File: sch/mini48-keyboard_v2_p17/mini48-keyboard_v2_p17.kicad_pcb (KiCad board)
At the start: 2 copper layers, 232 x 76 mm, 120 parts, among them SW1 SW_Push, SW10 SW_Push, SW11 SW_Push, SW12 SW_Push, SW13 SW_Push, SW14 SW_Push, SW15 SW_Push, SW16 SW_Push, SW17 SW_Push, SW18 SW_Push, SW19 SW_Push, SW2 SW_Push, SW20 SW_Push, SW21 SW_Push, SW22 SW_Push, SW23 SW_Push, SW24 SW_Push, SW25 SW_Push, SW26 SW_Push, SW27 SW_Push, SW28 SW_Push, SW29 SW_Push, SW3 SW_Push, SW30 SW_Push, SW31 SW_Push, SW32 SW_Push, SW33 SW_Push, SW34 SW_Push, SW35 SW_Push, SW36 SW_Push, SW37 SW_Push, SW38 SW_Push, SW39 SW_Push, SW4 SW_Push, SW40 SW_Push, SW41 SW_Push, SW42 SW_Push, SW43 SW_Push, SW44 SW_Push, SW45 SW_Push, SW46 SW_Push, SW47 SW_Push, SW48 SW_Push, SW5 SW_Push, SW6 SW_Push, SW7 SW_Push, SW8 SW_Push, SW9 SW_Push

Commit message: ざっくり配線しました。 pico と  ae-rp2040 を選択できるようにしました。
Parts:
- removed the REF** at (59.0, 57.0)
- removed the REF** at (210.0, 128.0)
- added D49: PMEG40T20ER, Diode_SMD:Nexperia_CFP3_SOD-123W, F.Cu at (250.6, 32.0)
- added J1: Conn_01x20, Connector_PinHeader_2.54mm:PinHeader_1x20_P2.54mm_Vertical, F.Cu at (139.1, 84.0)
- added J2: Conn_01x02, Connector_JST:JST_PH_B2B-PH-K_1x02_P2.00mm_Vertical, F.Cu at (250.8, 26.6)
- added U2: Pico, my_pico:pico_no_dbg_smd_th_p0.85, F.Cu at (221.9, 62.9)
- U1: footprint ae-rp2040:AE-RP2040 -> ae-rp2040:AE-RP2040_p0.85; moved to F.Cu
- moved REF** 195.3 mm to (111.0, 175.0)
- moved REF** 172.0 mm to (103.0, 174.0)
- moved REF** 168.3 mm to (132.0, 174.0)
- moved REF** 153.9 mm to (91.0, 174.0)
- moved REF** 138.3 mm to (79.0, 174.0)
- moved REF** 135.3 mm to (145.0, 187.0)
- moved REF** 131.6 mm to (119.0, 188.0)
- moved REF** 126.2 mm to (67.0, 174.0)
- moved REF** 120.5 mm to (98.0, 188.0)
- moved REF** 119.0 mm to (53.0, 174.0)
- moved REF** 116.5 mm to (41.0, 174.0)
- moved REF** 113.7 mm to (132.0, 187.0)
- moved REF** 110.5 mm to (78.0, 188.0)
- moved REF** 105.9 mm to (22.0, 178.0)
- moved REF** 103.0 mm to (57.0, 188.0)
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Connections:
- net /COL0 renamed /GPIO15
- net /COL1 renamed /GPIO14
- net /COL10 renamed /GPIO20
- net /COL11 renamed /GPIO21
- net /COL2 renamed /GPIO13
- net /COL3 renamed /GPIO12
- net /COL4 renamed /GPIO11
- net /COL5 renamed /GPIO10
- net /COL6 renamed /GPIO16
- net /COL7 renamed /GPIO17
- net /COL8 renamed /GPIO18
- net /COL9 renamed /GPIO19
- net /ROW0 renamed /GPIO2
- net /ROW1 renamed /GPIO3
- net /ROW2 renamed /GPIO4
- net /ROW3 renamed /GPIO5
- U1 pad 10: unconnected-(U1-GPIO8-Pad10) -> /GPIO8
- U1 pad 11: unconnected-(U1-GPIO9-Pad11) -> /GPIO9
- U1 pad 2: unconnected-(U1-GPIO0-Pad2) -> /GPIO0
- U1 pad 25: unconnected-(U1-GPIO22-Pad25) -> /GPIO22
- U1 pad 29: unconnected-(U1-GPIO26-Pad29) -> /GPIO26
- U1 pad 3: unconnected-(U1-GPIO1-Pad3) -> /GPIO1
- U1 pad 30: unconnected-(U1-GPIO27-Pad30) -> /GPIO27
- U1 pad 31: unconnected-(U1-GPIO28-Pad31) -> /GPIO28
- U1 pad 34: +3.3V -> unconnected-(U1-+3.3V-Pad34)
- U1 pad 8: unconnected-(U1-GPIO6-Pad8) -> /GPIO6
- U1 pad 9: unconnected-(U1-GPIO7-Pad9) -> /GPIO7
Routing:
- net /GPIO5: track 244.5 -> 355.3 mm
- net /GPIO2: track 322.2 -> 226.0 mm
- net /GPIO12: track 210.3 -> 129.5 mm, vias 1 -> 0
- net /GPIO11: track 187.8 -> 115.7 mm, vias 1 -> 0
- net /GPIO21: track 68.0 -> 138.6 mm
- net /GPIO15: track 244.6 -> 175.3 mm, vias 1 -> 0
- net /GPIO10: track 169.8 -> 101.0 mm, vias 1 -> 0
- net /GPIO13: track 211.7 -> 144.6 mm, vias 1 -> 0
- net /GPIO14: track 226.9 -> 161.3 mm, vias 1 -> 0
- net /GPIO4: track 275.5 -> 340.3 mm
- net /GPIO16: track 149.7 -> 93.0 mm, vias 1 -> 0
- net /GPIO20: track 69.3 -> 124.1 mm
- net /GPIO17: track 122.0 -> 84.7 mm, vias 1 -> 0
- net /GPIO19: track 91.1 -> 107.8 mm, vias 1 -> 0
- net /GPIO27: track 0.00 -> 15.7 mm
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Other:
- board size 232 x 76 mm -> 211 x 112 mm
- board text added: "mini48-keyboard_v2_p17"
- board text removed: "mini48-keyboard"

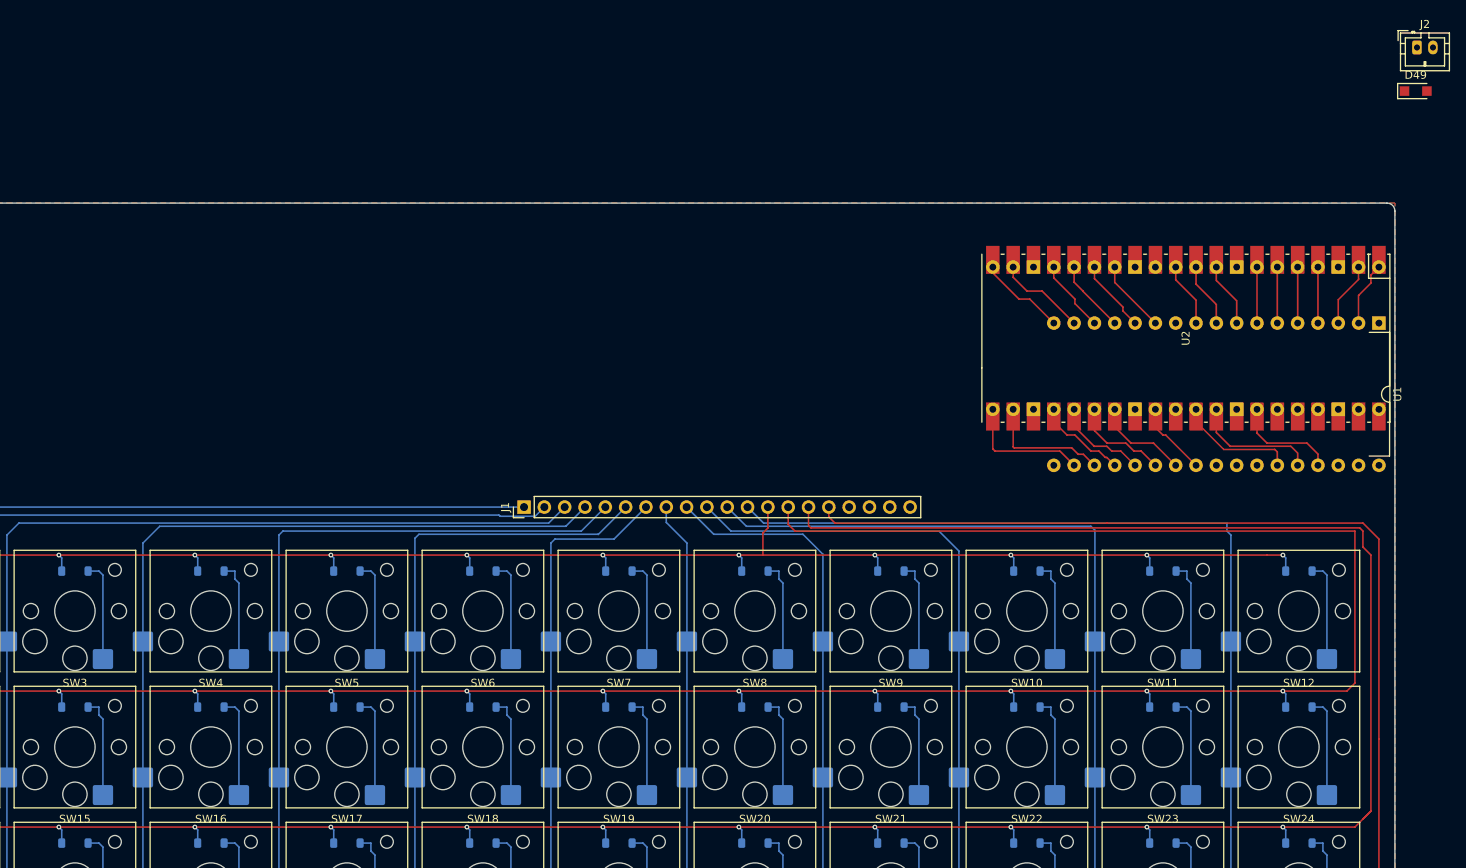
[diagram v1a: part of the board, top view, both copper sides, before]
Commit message: LCDのクロック線周りを微修正。
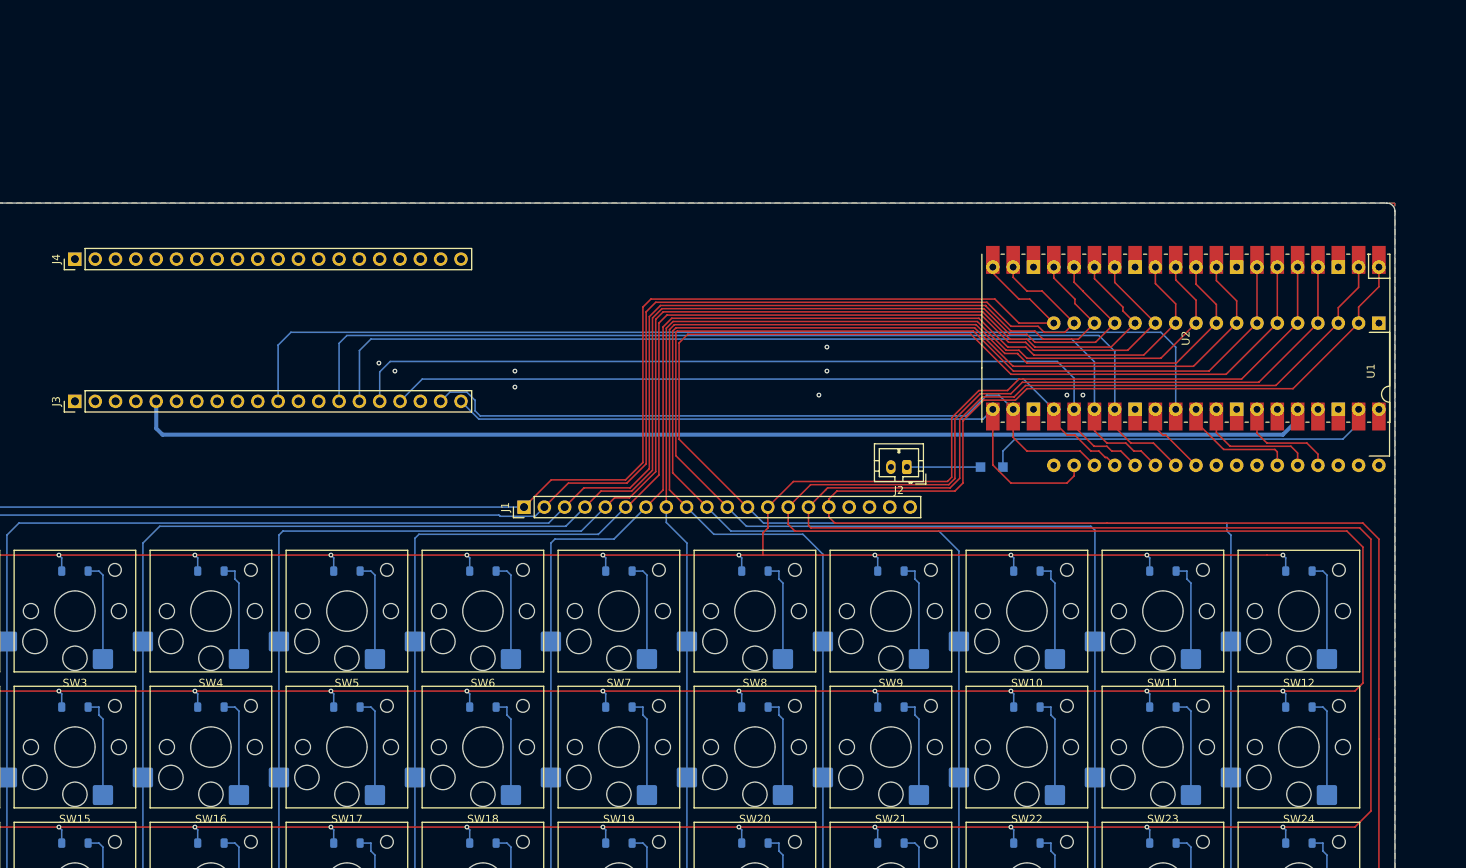
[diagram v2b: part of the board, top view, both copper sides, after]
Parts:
- added J3: Conn_01x20, Connector_PinHeader_2.54mm:PinHeader_1x20_P2.54mm_Vertical, F.Cu at (83.0, 70.8)
- added J4: Conn_01x20, Connector_PinHeader_2.54mm:PinHeader_1x20_P2.54mm_Vertical, F.Cu at (83.0, 53.0)
- D49: moved to B.Cu
- moved J2 82.6 mm to (187.0, 79.0), turned to 180 degrees
- moved D49 70.8 mm to (197.6, 79.0), turned to 180 degrees
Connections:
- D1 pad 1: /GPIO2 -> /GPIO3
- D10 pad 1: /GPIO2 -> /GPIO3
- D11 pad 1: /GPIO2 -> /GPIO3
- D12 pad 1: /GPIO2 -> /GPIO3
- D13 pad 1: /GPIO3 -> /GPIO2
- D14 pad 1: /GPIO3 -> /GPIO2
- D15 pad 1: /GPIO3 -> /GPIO2
- D16 pad 1: /GPIO3 -> /GPIO2
- D17 pad 1: /GPIO3 -> /GPIO2
- D18 pad 1: /GPIO3 -> /GPIO2
- D19 pad 1: /GPIO3 -> /GPIO2
- D2 pad 1: /GPIO2 -> /GPIO3
- D20 pad 1: /GPIO3 -> /GPIO2
- D21 pad 1: /GPIO3 -> /GPIO2
- D22 pad 1: /GPIO3 -> /GPIO2
- D23 pad 1: /GPIO3 -> /GPIO2
- D24 pad 1: /GPIO3 -> /GPIO2
- D25 pad 1: /GPIO4 -> /GPIO1
- D26 pad 1: /GPIO4 -> /GPIO1
- D27 pad 1: /GPIO4 -> /GPIO1
- D28 pad 1: /GPIO4 -> /GPIO1
- D29 pad 1: /GPIO4 -> /GPIO1
- D3 pad 1: /GPIO2 -> /GPIO3
- D30 pad 1: /GPIO4 -> /GPIO1
- D31 pad 1: /GPIO4 -> /GPIO1
- D32 pad 1: /GPIO4 -> /GPIO1
- D33 pad 1: /GPIO4 -> /GPIO1
- D34 pad 1: /GPIO4 -> /GPIO1
- D35 pad 1: /GPIO4 -> /GPIO1
- D36 pad 1: /GPIO4 -> /GPIO1
- D37 pad 1: /GPIO5 -> /GPIO0
- D38 pad 1: /GPIO5 -> /GPIO0
- D39 pad 1: /GPIO5 -> /GPIO0
- D4 pad 1: /GPIO2 -> /GPIO3
- D40 pad 1: /GPIO5 -> /GPIO0
- D41 pad 1: /GPIO5 -> /GPIO0
- D42 pad 1: /GPIO5 -> /GPIO0
- D43 pad 1: /GPIO5 -> /GPIO0
- D44 pad 1: /GPIO5 -> /GPIO0
- D45 pad 1: /GPIO5 -> /GPIO0
- D46 pad 1: /GPIO5 -> /GPIO0
- D47 pad 1: /GPIO5 -> /GPIO0
- D48 pad 1: /GPIO5 -> /GPIO0
- D5 pad 1: /GPIO2 -> /GPIO3
- D6 pad 1: /GPIO2 -> /GPIO3
- D7 pad 1: /GPIO2 -> /GPIO3
- D8 pad 1: /GPIO2 -> /GPIO3
- D9 pad 1: /GPIO2 -> /GPIO3
- J1 pad 10: /GPIO19 -> /GPIO6
- J1 pad 11: /GPIO20 -> /GPIO5
- J1 pad 12: /GPIO21 -> /GPIO4
- J1 pad 13: /GPIO2 -> /GPIO3
- J1 pad 14: /GPIO3 -> /GPIO2
- J1 pad 15: /GPIO4 -> /GPIO1
- J1 pad 16: /GPIO5 -> /GPIO0
- J1 pad 7: /GPIO16 -> /GPIO9
- J1 pad 8: /GPIO17 -> /GPIO8
- J1 pad 9: /GPIO18 -> /GPIO7
- SW10 pad 2: /GPIO19 -> /GPIO6
- SW11 pad 2: /GPIO20 -> /GPIO5
- SW12 pad 2: /GPIO21 -> /GPIO4
- SW19 pad 2: /GPIO16 -> /GPIO9
- SW20 pad 2: /GPIO17 -> /GPIO8
- SW21 pad 2: /GPIO18 -> /GPIO7
- SW22 pad 2: /GPIO19 -> /GPIO6
- SW23 pad 2: /GPIO20 -> /GPIO5
- SW24 pad 2: /GPIO21 -> /GPIO4
- SW31 pad 2: /GPIO16 -> /GPIO9
- SW32 pad 2: /GPIO17 -> /GPIO8
- SW33 pad 2: /GPIO18 -> /GPIO7
- SW34 pad 2: /GPIO19 -> /GPIO6
- SW35 pad 2: /GPIO20 -> /GPIO5
- SW36 pad 2: /GPIO21 -> /GPIO4
- SW43 pad 2: /GPIO16 -> /GPIO9
- SW44 pad 2: /GPIO17 -> /GPIO8
- SW45 pad 2: /GPIO18 -> /GPIO7
- SW46 pad 2: /GPIO19 -> /GPIO6
- SW47 pad 2: /GPIO20 -> /GPIO5
- SW48 pad 2: /GPIO21 -> /GPIO4
- SW7 pad 2: /GPIO16 -> /GPIO9
- SW8 pad 2: /GPIO17 -> /GPIO8
- SW9 pad 2: /GPIO18 -> /GPIO7
- U2 pad 30: unconnected-(U2-RUN-Pad30)_1 -> /RUN
- U2 pad 36: unconnected-(U2-3V3-Pad36) -> +3.3V
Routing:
- net /GPIO0: track 8.05 -> 437.2 mm, vias 0 -> 12
- net /GPIO1: track 8.05 -> 420.0 mm, vias 0 -> 12
- net /GPIO6: track 8.05 -> 202.8 mm
- net /GPIO7: track 8.05 -> 185.2 mm
- net /GPIO9: track 0.00 -> 176.6 mm
- net /GPIO2: track 226.0 -> 402.4 mm
- net /GPIO8: track 8.05 -> 169.6 mm
- net +3.3V: track 0.00 -> 148.6 mm
- net /GPIO5: track 355.3 -> 220.8 mm, vias 12 -> 0
- net /RUN: track 0.00 -> 128.4 mm
- net /GPIO4: track 340.3 -> 237.8 mm, vias 12 -> 0
- net /GPIO11: track 115.7 -> 206.2 mm
- net /GPIO10: track 101.0 -> 191.5 mm
- net /GPIO12: track 129.5 -> 219.9 mm
- net /GPIO13: track 144.6 -> 235.0 mm
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
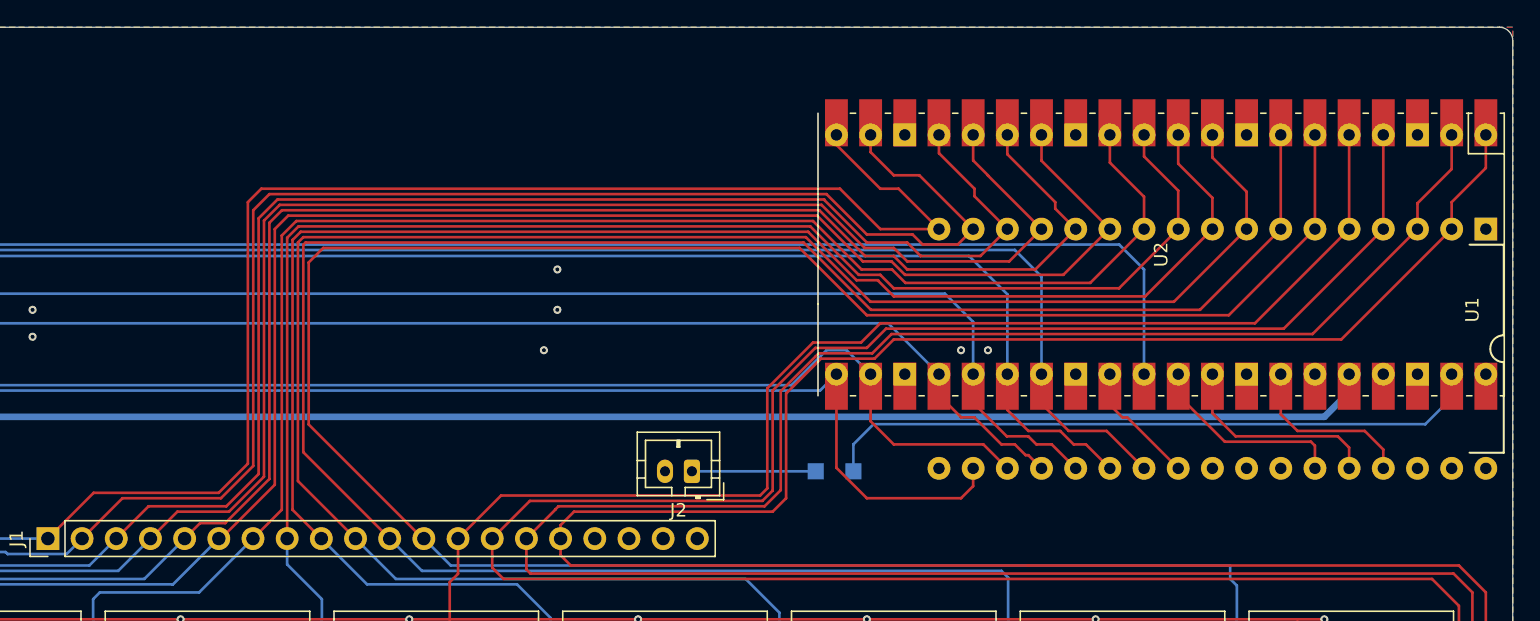
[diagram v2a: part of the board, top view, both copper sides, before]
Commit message: マイコンボードを pico のみに変更しました。 スイッチのシートの名前を変えました。
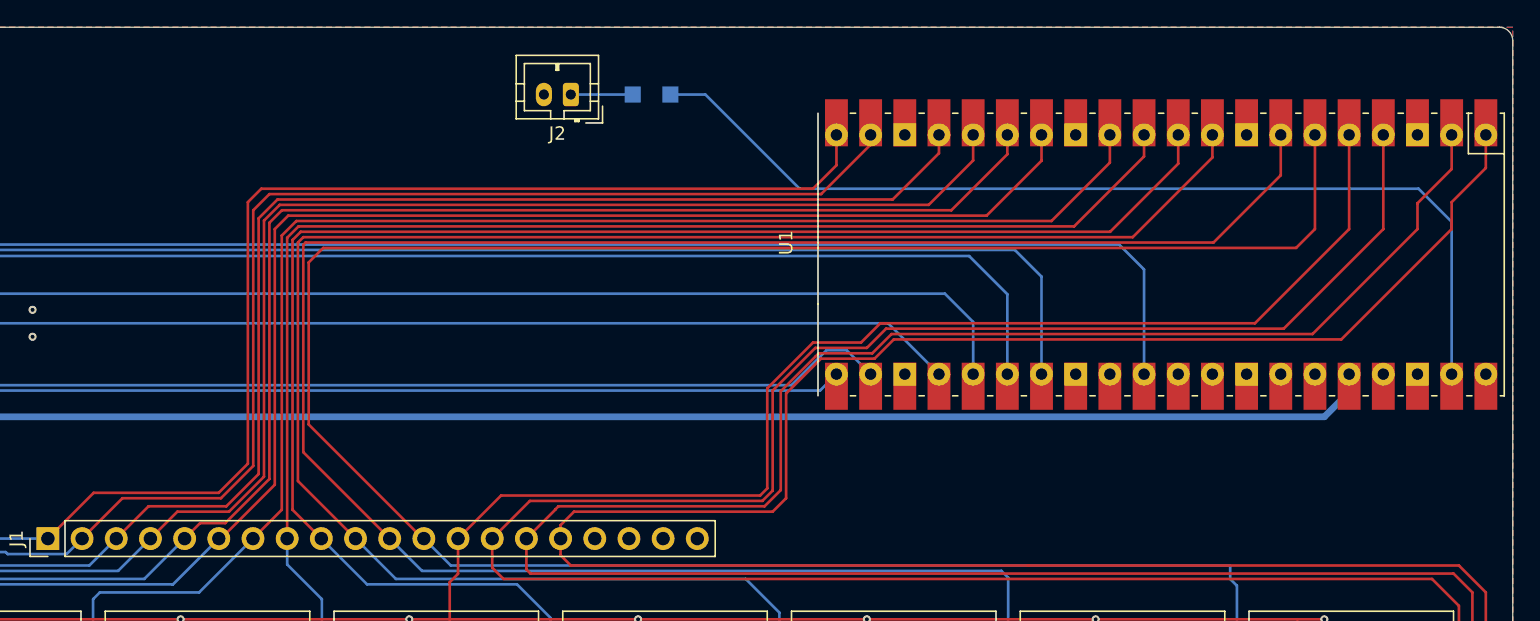
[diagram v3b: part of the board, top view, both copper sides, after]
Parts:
- removed U2: Pico, my_pico:pico_no_dbg_smd_th_p0.85
- U1: value ~ -> Pico; footprint ae-rp2040:AE-RP2040_p0.85 -> my_pico:pico_no_dbg_smd_th_p0.85
- moved D49 31.1 mm to (184.0, 51.0)
- moved J2 29.4 mm to (178.0, 51.0)
- moved U1 24.2 mm to (221.9, 62.9)
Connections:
- U1 pad 1: unconnected-(U1-+5V-Pad1) -> /GPIO0
- U1 pad 10: /GPIO8 -> /GPIO7
- U1 pad 11: /GPIO9 -> /GPIO8
- U1 pad 12: /GPIO10 -> /GPIO9
- U1 pad 13: /GPIO11 -> GND
- U1 pad 14: /GPIO12 -> /GPIO10
- U1 pad 15: /GPIO13 -> /GPIO11
- U1 pad 16: /GPIO14 -> /GPIO12
- U1 pad 17: /GPIO15 -> /GPIO13
- U1 pad 19: /GPIO16 -> /GPIO14
- U1 pad 2: /GPIO0 -> /GPIO1
- U1 pad 20: /GPIO17 -> /GPIO15
- U1 pad 21: /GPIO18 -> /GPIO16
- U1 pad 22: /GPIO19 -> /GPIO17
- U1 pad 23: /GPIO20 -> GND
- U1 pad 24: /GPIO21 -> /GPIO18
- U1 pad 25: /GPIO22 -> /GPIO19
- U1 pad 26: unconnected-(U1-GPIO23-Pad26) -> /GPIO20
- U1 pad 27: unconnected-(U1-GPIO24-Pad27) -> /GPIO21
- U1 pad 28: unconnected-(U1-GPIO25-Pad28) -> GND
- U1 pad 29: /GPIO26 -> unconnected-(U1-GPIO22-Pad29)
- U1 pad 3: /GPIO1 -> GND
- U1 pad 30: /GPIO27 -> /RUN
- U1 pad 31: /GPIO28 -> unconnected-(U1-GPIO26_ADC0-Pad31)
- U1 pad 8: /GPIO6 -> GND
- U1 pad 9: /GPIO7 -> /GPIO6
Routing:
- net Net-(D49-K): track 49.7 -> 73.3 mm
- net /GPIO16: track 87.7 -> 67.9 mm
- net /GPIO14: track 251.3 -> 232.6 mm
- net /GPIO15: track 265.0 -> 248.1 mm
- net /GPIO27: track 15.7 -> 0.00 mm
- net /GPIO17: track 91.0 -> 75.9 mm
- net /GPIO26: track 15.0 -> 0.00 mm
- net /GPIO11: track 206.2 -> 192.1 mm
- net /GPIO13: track 235.0 -> 221.0 mm
- net /GPIO10: track 191.5 -> 177.7 mm
- net /GPIO12: track 219.9 -> 206.3 mm
- net /GPIO28: track 13.1 -> 0.00 mm
- net /GPIO20: track 118.0 -> 105.9 mm
- net /GPIO21: track 124.5 -> 112.7 mm
- net /GPIO19: track 107.5 -> 95.8 mm
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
